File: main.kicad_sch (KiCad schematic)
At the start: 3 parts

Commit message: Lots of changfes
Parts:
- renumbered D11 to D3
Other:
- sheet BMS ports: added INT_5V, TOP; removed AFE_5V, BATT+
- sheet external_io ports: added {BMS_SIG}; removed none
- sheet microcontroller ports: added USB_D+, USB_D-; removed USB_DM, USB_DP
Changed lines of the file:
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@@
 		(color 0 0 0 0)
 	)
+	(junction
+		(at 158.75 83.82)
+		(diameter 0)
+		(color 0 0 0 0)
+	)
 	(wire
 		(pts
@@
 	(bus
 		(pts
-			(xy 158.75 77.47) (xy 158.75 90.17)
+			(xy 158.75 77.47) (xy 158.75 83.82)
 		)
 		(stroke
@@
 		)
 	)
+	(bus
+		(pts
+			(xy 158.75 83.82) (xy 194.31 83.82)
+		)
+		(stroke
+			(width 0)
+			(type default)
+		)
+	)
 	(wire
 		(pts
@@
 		)
 	)
+	(bus
+		(pts
+			(xy 172.72 128.27) (xy 194.31 128.27)
+		)
+		(stroke
+			(width 0)
+			(type default)
+		)
+	)
 	(wire
 		(pts
@@
 		)
 	)
+	(bus
+		(pts
+			(xy 158.75 83.82) (xy 158.75 90.17)
+		)
+		(stroke
+			(width 0)
+			(type default)
+		)
+	)
 	(wire
 		(pts
@@
 		)
 	)
+	(bus
+		(pts
+			(xy 172.72 74.93) (xy 172.72 128.27)
+		)
+		(stroke
+			(width 0)
+			(type default)
+		)
+	)
 	(wire
 		(pts
@@
 	(bus
 		(pts
-			(xy 172.72 74.93) (xy 172.72 128.27)
-		)
-		(stroke
-			(width 0)
-			(type default)
-		)
-	)
-	(bus
-		(pts
 			(xy 170.18 72.39) (xy 194.31 72.39)
 		)
@@
 		(pts
 			(xy 105.41 114.3) (xy 128.27 114.3)
-		)
-		(stroke
-			(width 0)
-			(type default)
-		)
-	)
-	(bus
-		(pts
-			(xy 172.72 128.27) (xy 194.31 128.27)
 		)
 		(stroke
@@
 		(on_board yes)
 		(dnp no)
-		(property "Reference" "D11"
+		(property "Reference" "D3"
 			(at 72.39 69.85 0)
 			(effects
@@
 			(project "BMS"
 				(path "/124184ba-5d68-4d9f-8da6-acc6720ab30b/93f9b420-7cce-46a9-9201-666f07a18f85"
-					(reference "D11")
+					(reference "D3")
 					(unit 1)
 				)
@@
 			(project "BMS"
 				(path "/124184ba-5d68-4d9f-8da6-acc6720ab30b/93f9b420-7cce-46a9-9201-666f07a18f85"
-					(page "10")
+					(page "6")
 				)
 			)
@@
 			)
 		)
+		(pin "{BMS_SIG}" bidirectional
+			(at 194.31 83.82 180)
+			(effects
+				(font
+					(size 1.27 1.27)
+				)
+				(justify left)
+			)
+		)
 		(instances
 			(project "BMS"
 				(path "/124184ba-5d68-4d9f-8da6-acc6720ab30b/93f9b420-7cce-46a9-9201-666f07a18f85"
-					(page "2")
+					(page "4")
 				)
 			)
@@
 			(project "BMS"
 				(path "/124184ba-5d68-4d9f-8da6-acc6720ab30b/93f9b420-7cce-46a9-9201-666f07a18f85"
-					(page "#")
+					(page "7")
 				)
 			)
@@
 			)
 		)
-		(pin "USB_DP" bidirectional
-			(at 170.18 52.07 0)
-			(effects
-				(font
-					(size 1.27 1.27)
-				)
-				(justify right)
-			)
-		)
 		(pin "{I2C}" bidirectional
 			(at 170.18 74.93 0)
@@
 			)
 		)
-		(pin "USB_DM" bidirectional
-			(at 170.18 54.61 0)
-			(effects
-				(font
-					(size 1.27 1.27)
-				)
-				(justify right)
-			)
-		)
 		(pin "{SERIAL}" bidirectional
 			(at 170.18 62.23 0)
@@
 		(pin "{SWD}" bidirectional
 			(at 170.18 72.39 0)
+			(effects
+				(font
+					(size 1.27 1.27)
+				)
+				(justify right)
+			)
+		)
+		(pin "USB_D+" bidirectional
+			(at 170.18 52.07 0)
+			(effects
+				(font
+					(size 1.27 1.27)
+				)
+				(justify right)
+			)
+		)
+		(pin "USB_D-" bidirectional
+			(at 170.18 54.61 0)
 			(effects
 				(font
@@
 			(project "BMS"
 				(path "/124184ba-5d68-4d9f-8da6-acc6720ab30b/93f9b420-7cce-46a9-9201-666f07a18f85"
-					(page "8")
+					(page "5")
 				)
 			)
@@
 			)
 		)
-		(pin "BATT+" output
-			(at 128.27 114.3 180)
-			(effects
-				(font
-					(size 1.27 1.27)
-				)
-				(justify left)
-			)
-		)
 		(pin "BATT-" output
 			(at 128.27 116.84 180)
@@
 			)
 		)
-		(pin "AFE_5V" output
-			(at 128.27 92.71 180)
-			(effects
-				(font
-					(size 1.27 1.27)
-				)
-				(justify left)
-			)
-		)
 		(pin "PACK+" output
 			(at 170.18 114.3 0)
@@
 				)
 				(justify right)
+			)
+		)
+		(pin "INT_5V" output
+			(at 128.27 92.71 180)
+			(effects
+				(font
+					(size 1.27 1.27)
+				)
+				(justify left)
+			)
+		)
+		(pin "TOP" input
+			(at 128.27 114.3 180)
+			(effects
+				(font
+					(size 1.27 1.27)
+				)
+				(justify left)
 			)
 		)
@@
 			(project "BMS"
 				(path "/124184ba-5d68-4d9f-8da6-acc6720ab30b/93f9b420-7cce-46a9-9201-666f07a18f85"
-					(page "#")
-				)
-			)
+					(page "8")
+				)
+			)

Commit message: Placement
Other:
- added sheet NTC Inputs (ntc.kicad_sch)
- sheet cell_inputs ports: added none; removed NTC1, NTC2, NTC3, NTC4

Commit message: Pushing
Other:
- sheet BMS ports: added none; removed NTC4
- sheet NTC Inputs ports: added none; removed NTC4
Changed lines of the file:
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@@
 	(wire
 		(pts
-			(xy 105.41 101.6) (xy 128.27 101.6)
+			(xy 105.41 100.33) (xy 128.27 100.33)
 		)
 		(stroke
@@
 	(wire
 		(pts
-			(xy 105.41 99.06) (xy 128.27 99.06)
+			(xy 105.41 97.79) (xy 128.27 97.79)
 		)
 		(stroke
@@
 	(wire
 		(pts
-			(xy 105.41 93.98) (xy 128.27 93.98)
-		)
-		(stroke
-			(width 0)
-			(type default)
-		)
-	)
-	(wire
-		(pts
 			(xy 105.41 137.16) (xy 128.27 137.16)
 		)
@@
 	(wire
 		(pts
-			(xy 105.41 96.52) (xy 128.27 96.52)
+			(xy 105.41 95.25) (xy 128.27 95.25)
 		)
 		(stroke
@@
 		)
 		(pin "NTC1" output
-			(at 105.41 101.6 0)
+			(at 105.41 100.33 0)
 			(effects
 				(font
@@
 		)
 		(pin "NTC2" output
-			(at 105.41 99.06 0)
+			(at 105.41 97.79 0)
 			(effects
 				(font
@@
 		)
 		(pin "NTC3" output
-			(at 105.41 96.52 0)
-			(effects
-				(font
-					(size 1.27 1.27)
-				)
-				(justify right)
-			)
-		)
-		(pin "NTC4" output
-			(at 105.41 93.98 0)
+			(at 105.41 95.25 0)
 			(effects
 				(font
@@
 		)
 		(pin "NTC1" input
-			(at 128.27 101.6 180)
+			(at 128.27 100.33 180)
 			(effects
 				(font
@@
 		)
 		(pin "NTC2" input
-			(at 128.27 99.06 180)
+			(at 128.27 97.79 180)
 			(effects
 				(font
@@
 		)
 		(pin "NTC3" input
-			(at 128.27 96.52 180)
-			(effects
-				(font
-					(size 1.27 1.27)
-				)
-				(justify left)
-			)
-		)
-		(pin "NTC4" input
-			(at 128.27 93.98 180)
-			(effects
-				(font
+			(at 128.27 95.25 180)
+			(effects
+				(font

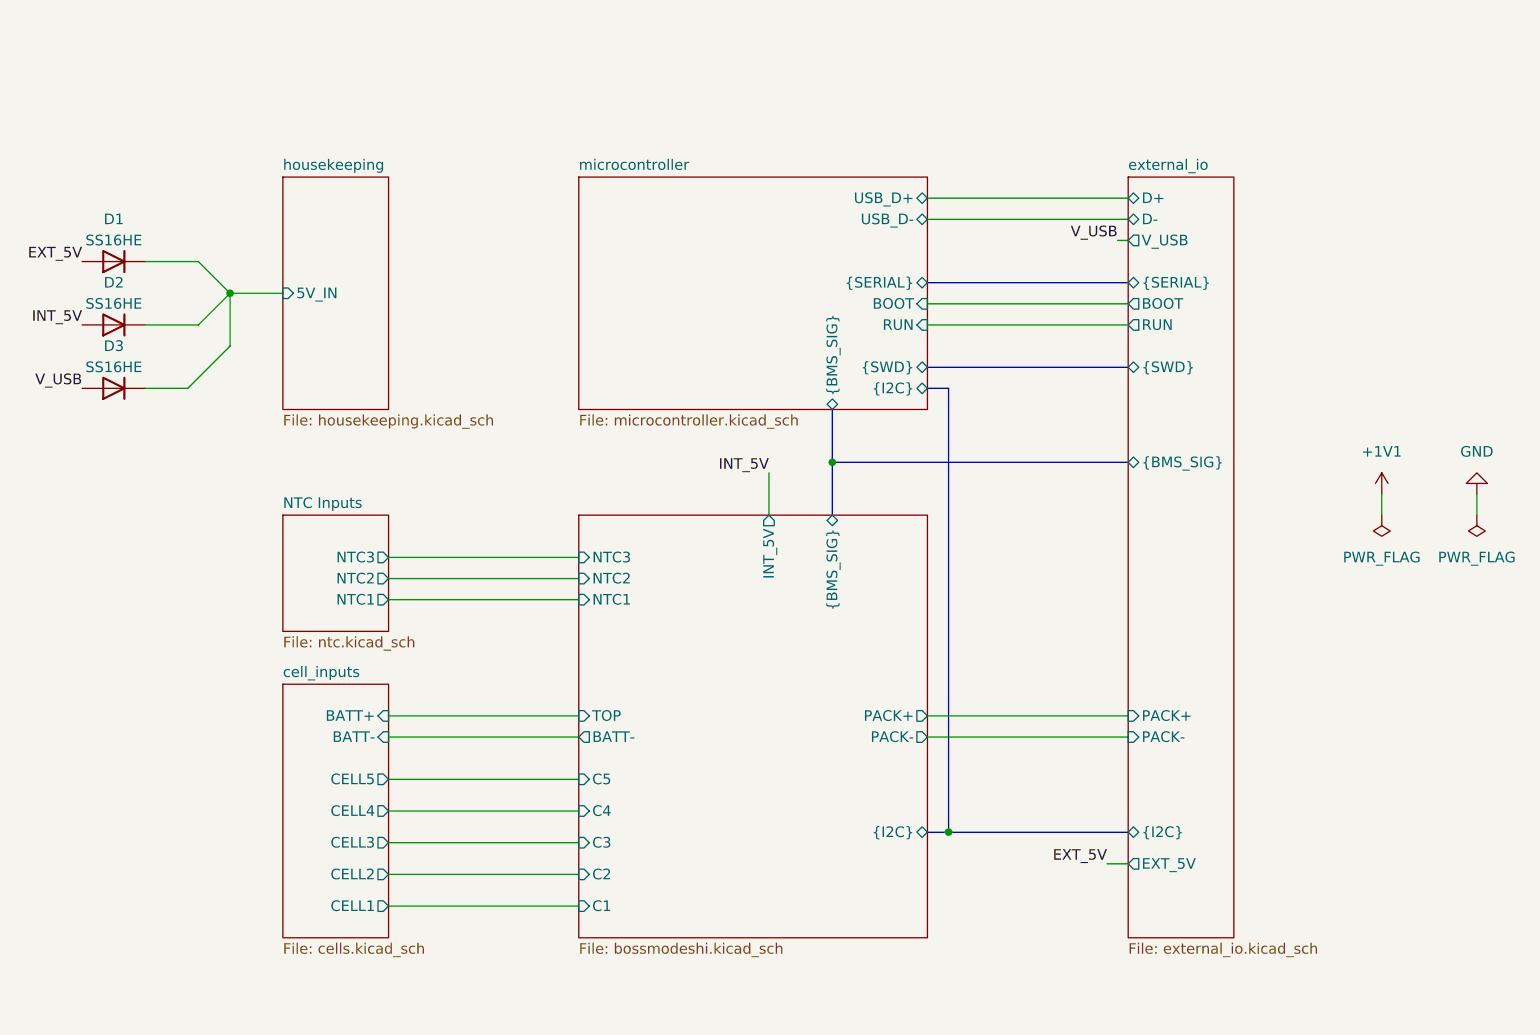
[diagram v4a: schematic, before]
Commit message: Adding in signals and cleaning up schematic
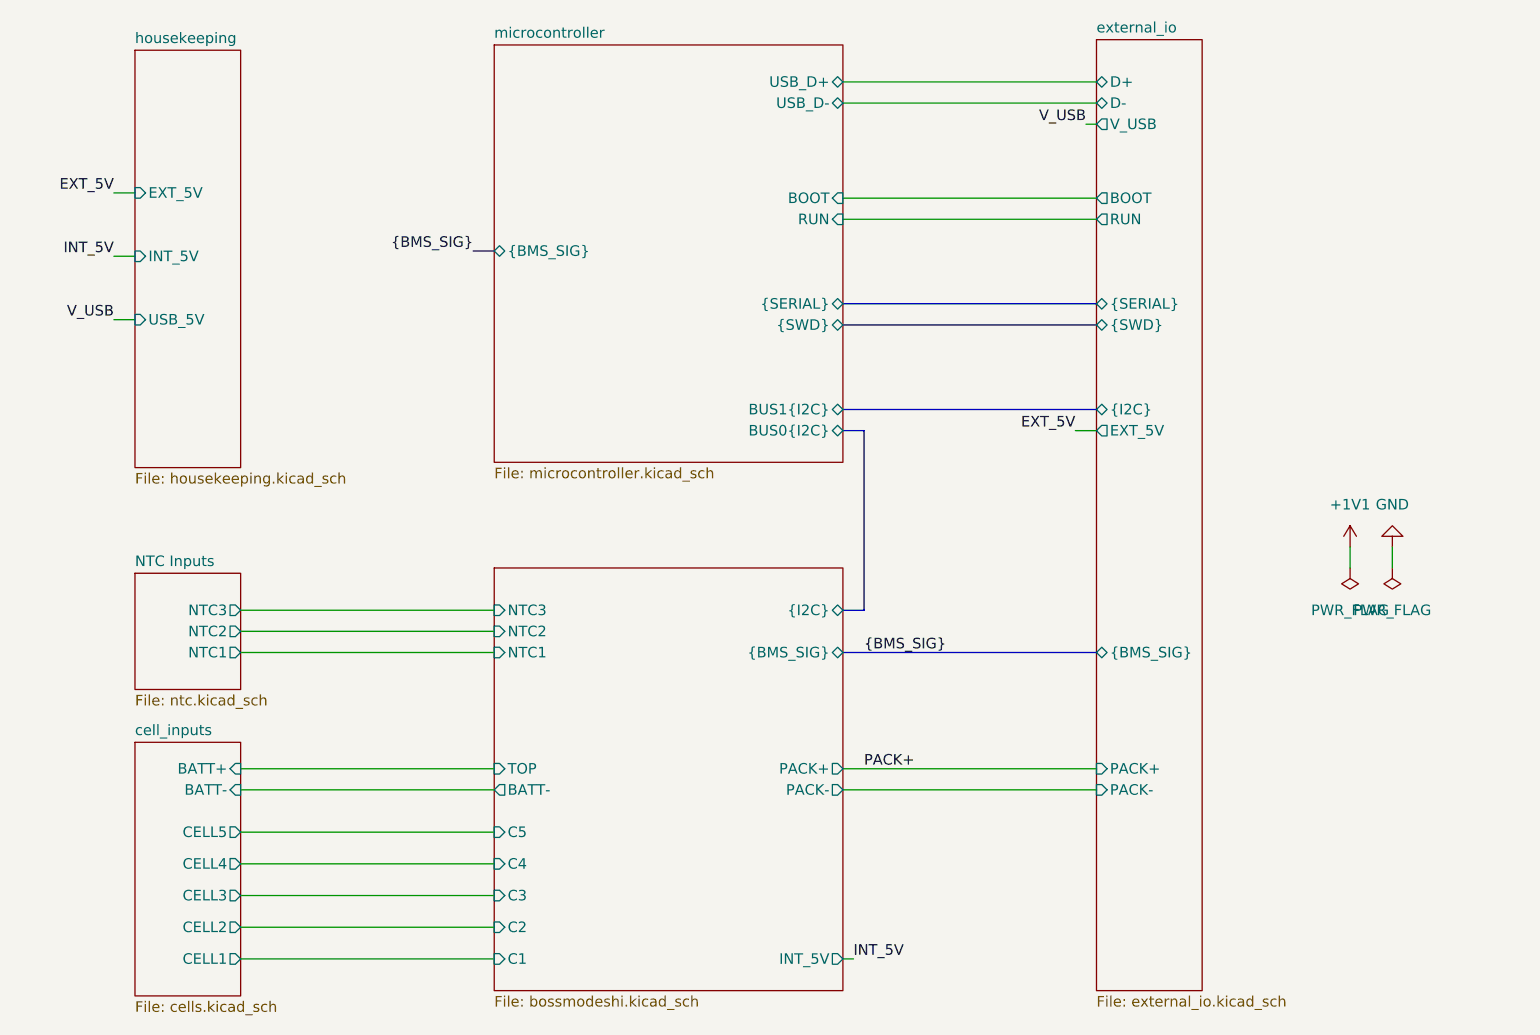
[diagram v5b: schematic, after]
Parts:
- removed D1, D2, D3: SS16HE, Diode_SMD:D_SOD-323F, symbol Device:D
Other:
- sheet housekeeping ports: added EXT_5V, INT_5V, USB_5V; removed 5V_IN
- sheet microcontroller ports: added BUS0{I2C}, BUS1{I2C}; removed {I2C}

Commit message: Redoing layout
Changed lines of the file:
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@@
 	(wire
 		(pts
-			(xy 72.39 51.435) (xy 74.93 51.435)
+			(xy 72.39 52.07) (xy 74.93 52.07)
 		)
 		(stroke
@@
 	(wire
 		(pts
-			(xy 72.39 59.055) (xy 74.93 59.055)
+			(xy 72.39 59.69) (xy 74.93 59.69)
 		)
 		(stroke
@@
 	(wire
 		(pts
-			(xy 72.39 66.675) (xy 74.93 66.675)
+			(xy 72.39 67.31) (xy 74.93 67.31)
 		)
 		(stroke
@@
 	)
 	(label "V_USB"
-		(at 72.39 66.675 180)
+		(at 72.39 67.31 180)
 		(effects
 			(font
@@
 	)
 	(label "EXT_5V"
-		(at 72.39 51.435 180)
+		(at 72.39 52.07 180)
 		(effects
 			(font
@@
 	)
 	(label "INT_5V"
-		(at 72.39 59.055 180)
+		(at 72.39 59.69 180)
 		(effects
 			(font
@@
 	)
 	(sheet
-		(at 74.93 34.29)
+		(at 74.93 34.925)
 		(size 12.7 50.165)
 		(exclude_from_sim no)
@@
 		)
 		(property "Sheetname" "housekeeping"
-			(at 74.93 33.5784 0)
+			(at 74.93 34.2134 0)
 			(effects
 				(font
@@
 		)
 		(property "Sheetfile" "housekeeping.kicad_sch"
-			(at 74.93 85.0396 0)
+			(at 74.93 85.6746 0)
 			(effects
 				(font
@@
 		)
 		(pin "EXT_5V" input
-			(at 74.93 51.435 180)
+			(at 74.93 52.07 180)
 			(effects
 				(font
@@
 		)
 		(pin "INT_5V" input
-			(at 74.93 59.055 180)
+			(at 74.93 59.69 180)
 			(effects
 				(font
@@
 		)
 		(pin "USB_5V" input
-			(at 74.93 66.675 180)
-			(effects
-				(font
+			(at 74.93 67.31 180)
+			(effects
+				(font

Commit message: prepaing for production
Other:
- sheet external_io ports: added BMS{I2C}; removed none
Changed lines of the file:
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@@
 	(generator_version "9.0")
 	(paper "A4")
+	(junction
+		(at 162.56 101.6)
+		(diameter 0)
+		(color 0 0 0 0)
+	)
 	(bus
 		(pts
@@
 		(pts
 			(xy 160.02 38.1) (xy 190.5 38.1)
+		)
+		(stroke
+			(width 0)
+			(type default)
+		)
+	)
+	(bus
+		(pts
+			(xy 162.56 101.6) (xy 190.5 101.6)
 		)
 		(stroke
@@
 			(effects
 				(font
+					(size 1.27 1.27)
+				)
+				(justify left)
+			)
+		)
+		(pin "BMS{I2C}" bidirectional
+			(at 190.5 101.6 180)
+			(effects
+				(font
